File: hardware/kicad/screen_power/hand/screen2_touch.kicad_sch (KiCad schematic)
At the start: 7 parts, among them J201 PI USB / XH4, J202 TOUCH / XH4, K201 IM02TS, Q201 2N7000

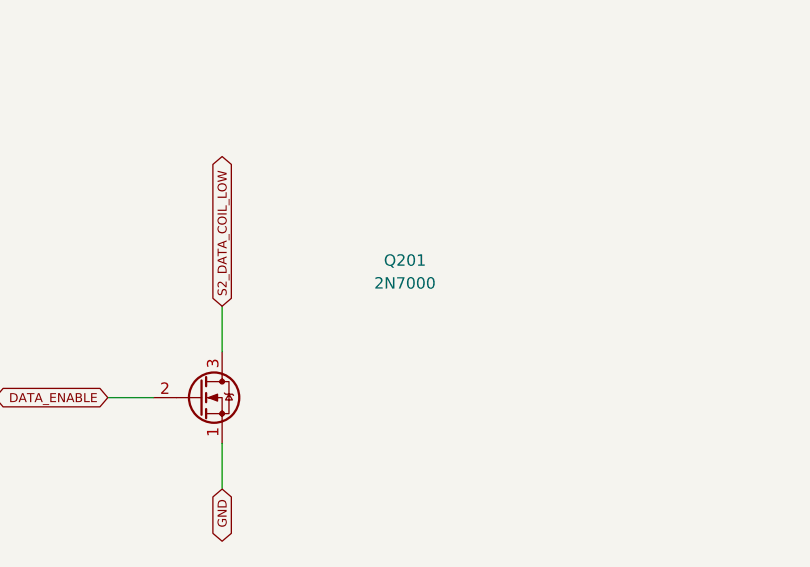
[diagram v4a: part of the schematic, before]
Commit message: fix(hardware): strengthen screen gate drive and finish PCB copper
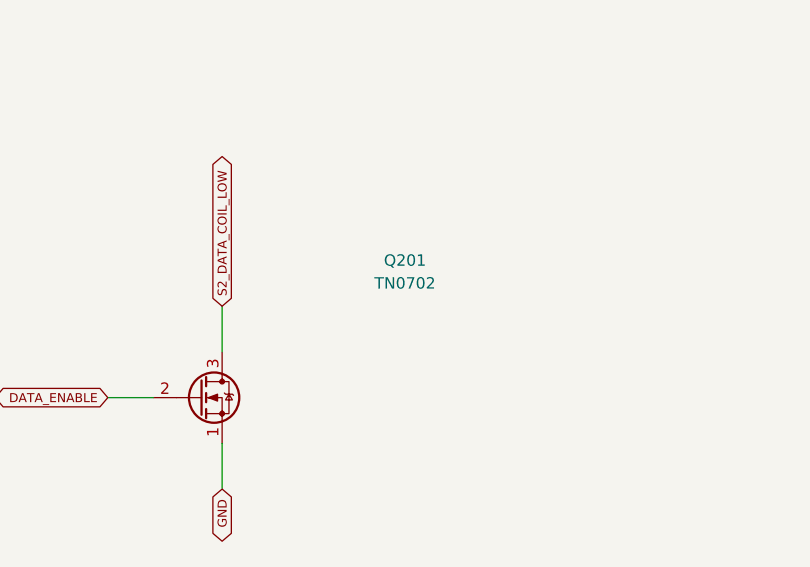
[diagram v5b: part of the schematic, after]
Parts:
- Q201: value 2N7000 -> TN0702; MPN 2N7000 -> TN0702N3-G
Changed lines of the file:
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@@
   (title_block
     (title "Segno screen power / hand / screen2 touch")
-    (rev "K prototype")
+    (rev "L prototype")
     (comment 1 "Discrete 5V switch. Host VBUS powers only its own signal relay coil.")
     (comment 2 "Physical verification required before release."))
@@
         (font
           (size 1.27 1.27))))
-    (property "Value" "2N7000"
+    (property "Value" "TN0702"
       (at 276.86 101.60000000000001 0)
       (effects
@@
           (size 1.27 1.27))
         (hide yes)))
-    (property "MPN" "2N7000"
+    (property "MPN" "TN0702N3-G"
       (at 276.86 114.3 0)
       (effects

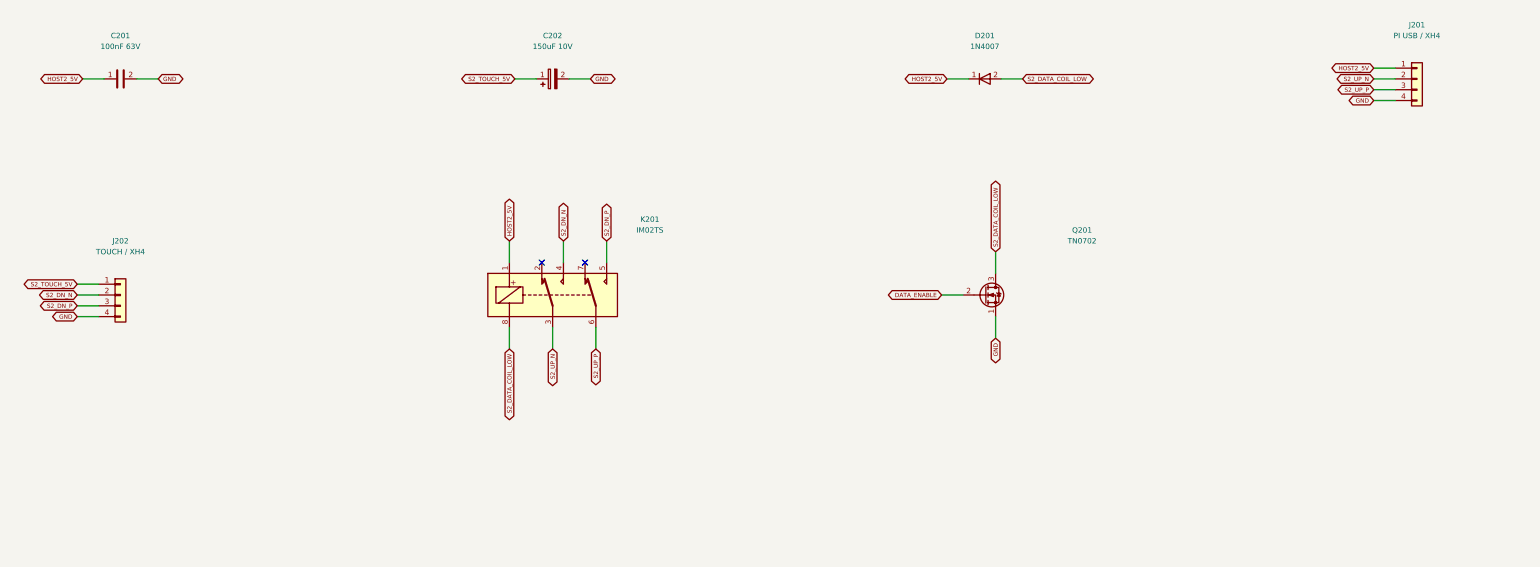
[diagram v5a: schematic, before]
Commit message: fix(hardware): correct USB relay power source and assess revised routing
Prepare Revision M schematic, low-current host sensing and shield drain pads. Keep screen manufacturing on hold pending the revised native layout and complete release validation.
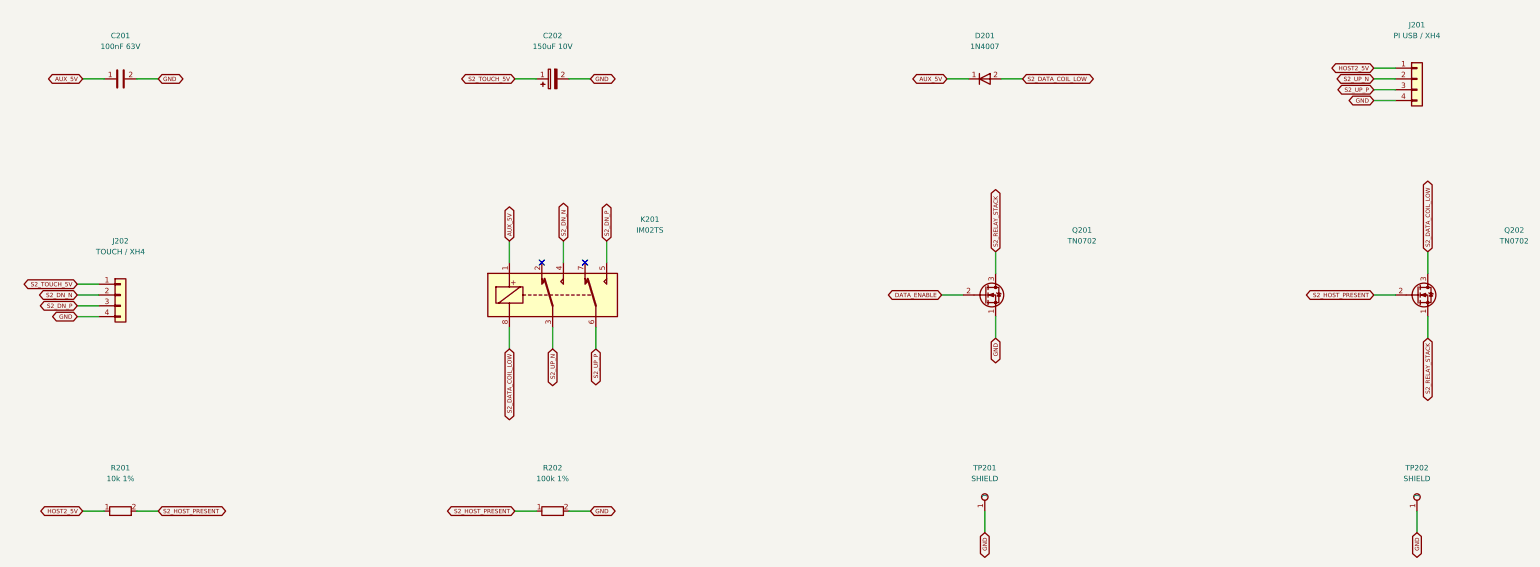
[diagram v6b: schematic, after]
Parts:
- added Q202: TN0702, Package_TO_SOT_THT:TO-92_Inline_Wide, symbol screen_symbols:Transistor_FET_2N7000
- added R201: 10k 1%, Resistor_THT:R_Axial_DIN0207_L6.3mm_D2.5mm_P10.16mm_Horizontal, symbol screen_symbols:Device_R
- added R202: 100k 1%, Resistor_THT:R_Axial_DIN0207_L6.3mm_D2.5mm_P10.16mm_Horizontal, symbol screen_symbols:Device_R
- added TP201, TP202: SHIELD, TestPoint:TestPoint_THTPad_D2.0mm_Drill1.0mm, symbol screen_symbols:Connector_TestPoint
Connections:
- net GND: now also R202.2, TP201.1, TP202.1
- net HOST2_5V: now also R201.1; no longer C201.1, D201.1 (K), K201.1
- net S2_DATA_COIL_LOW: now also Q202.3 (D); no longer Q201.3 (D)
- new net AUX_5V: C201.1, D201.1 (K), K201.1
- new net S2_HOST_PRESENT: Q202.2 (G), R201.2, R202.1
- new net S2_RELAY_STACK: Q201.3 (D), Q202.1 (S)

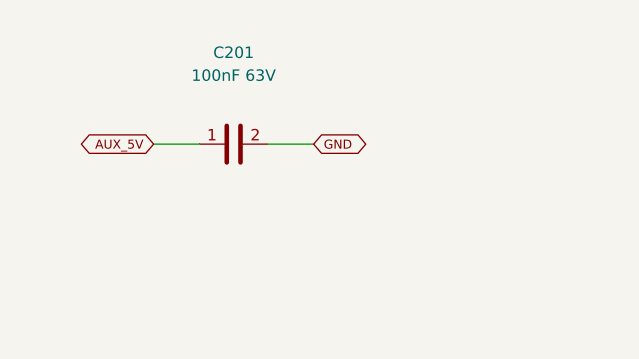
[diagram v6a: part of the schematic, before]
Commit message: feat(hardware): lower screen power cost and finish copper contours
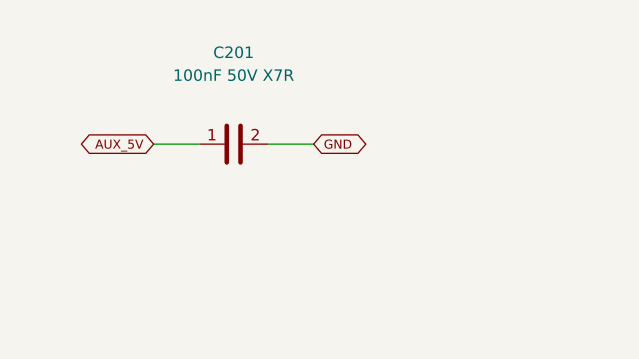
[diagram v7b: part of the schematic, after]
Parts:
- C201: value 100nF 63V -> 100nF 50V X7R; footprint Capacitor_THT:C_Rect_L7.2mm_W2.5mm_P5.00mm -> Capacitor_THT:C_Disc_D7.5mm_W4.4mm_P5.00mm; MPN MKS2C031001A00KSSD -> K104K10X7RF53H5
- D201: MPN 1N4007-E3/54 -> 1N4007G
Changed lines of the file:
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@@
   (title_block
     (title "Segno screen power / hand / screen2 touch")
-    (rev "M prototype")
-    (comment 1 "AUX-powered relays; each host VBUS supplies only its presence detector.")
-    (comment 2 "Physical verification required before release."))
+    (rev "N prototype")
+    (comment 1 "One normally open contact switches AUX; every board load sits behind F1.")
+    (comment 2 "AUX-powered relays; each host VBUS supplies only its presence detector.")
+    (comment 3 "Physical verification required before release."))
   (wire
     (pts
@@
         (font
           (size 1.27 1.27))))
-    (property "Value" "100nF 63V"
+    (property "Value" "100nF 50V X7R"
       (at 50.8 55.88 90)
       (effects
         (font
           (size 1.27 1.27))))
-    (property "Footprint" "Capacitor_THT:C_Rect_L7.2mm_W2.5mm_P5.00mm"
+    (property "Footprint" "Capacitor_THT:C_Disc_D7.5mm_W4.4mm_P5.00mm"
       (at 50.8 63.5 90)
       (effects
@@
           (size 1.27 1.27))
         (hide yes)))
-    (property "MPN" "MKS2C031001A00KSSD"
+    (property "MPN" "K104K10X7RF53H5"
       (at 50.8 63.5 90)
       (effects
@@
           (size 1.27 1.27))
         (hide yes)))
-    (property "MPN" "1N4007-E3/54"
+    (property "MPN" "1N4007G"
       (at 254.0 63.5 0)
       (effects

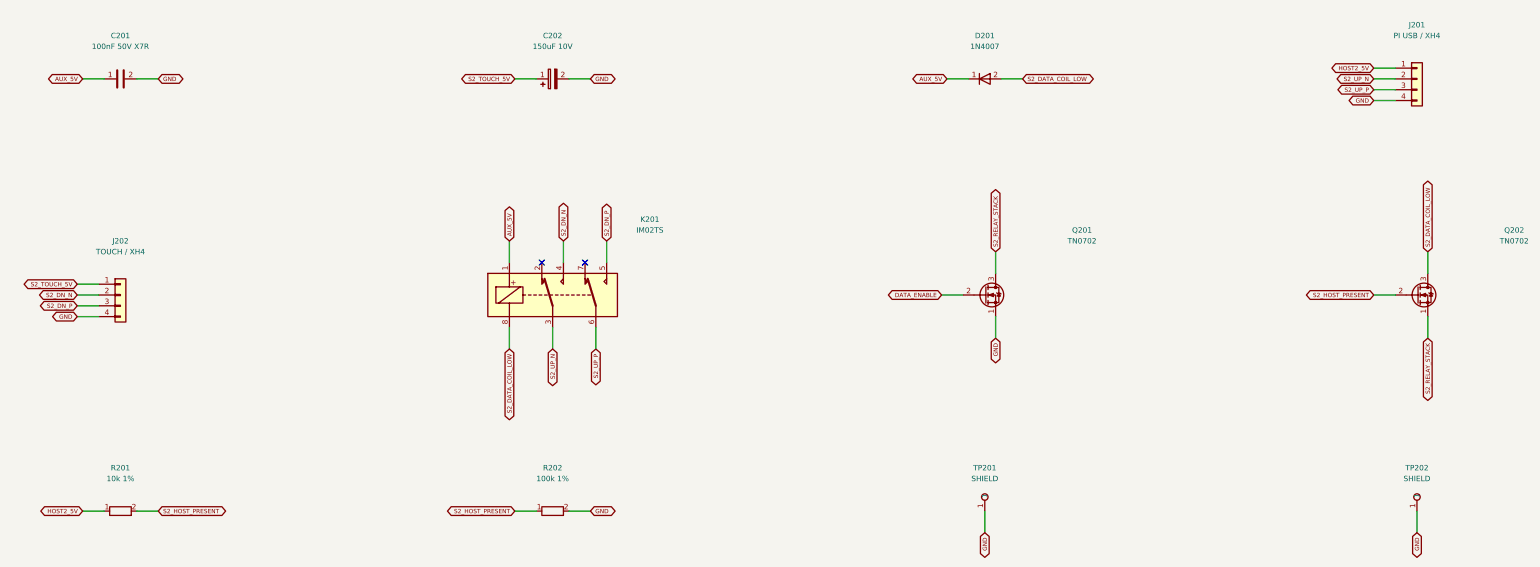
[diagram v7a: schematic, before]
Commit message: feat(hardware): carry USB shields through removable XH5 plugs
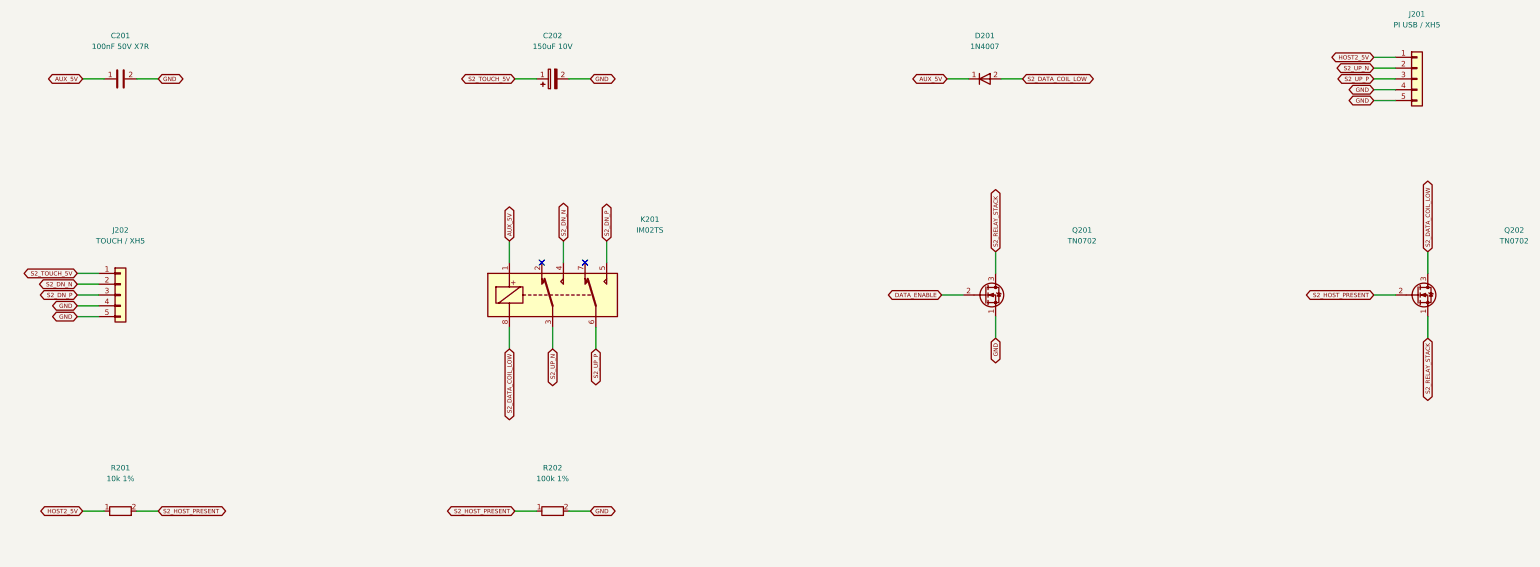
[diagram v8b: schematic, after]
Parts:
- removed TP201, TP202: SHIELD, TestPoint:TestPoint_THTPad_D2.0mm_Drill1.0mm, symbol screen_symbols:Connector_TestPoint
- J201: value PI USB / XH4 -> PI USB / XH5; footprint Connector_JST:JST_XH_B4B-XH-A_1x04_P2.50mm_Vertical -> Connector_JST:JST_XH_B5B-XH-A_1x05_P2.50mm_Vertical; symbol screen_symbols:Connector_Generic_Conn_01x04 -> screen_symbols:Connector_Generic_Conn_01x05; MPN B4B-XH-A(LF)(SN) -> B5B-XH-A(LF)(SN)
- J202: value TOUCH / XH4 -> TOUCH / XH5; footprint Connector_JST:JST_XH_B4B-XH-A_1x04_P2.50mm_Vertical -> Connector_JST:JST_XH_B5B-XH-A_1x05_P2.50mm_Vertical; symbol screen_symbols:Connector_Generic_Conn_01x04 -> screen_symbols:Connector_Generic_Conn_01x05; MPN B4B-XH-A(LF)(SN) -> B5B-XH-A(LF)(SN)
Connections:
- net GND: now also J201.5 (Pin_5), J202.5 (Pin_5)
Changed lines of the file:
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@@
   (title_block
     (title "Segno screen power / hand / screen2 touch")
-    (rev "N prototype")
+    (rev "O prototype")
     (comment 1 "One normally open contact switches AUX; every board load sits behind F1.")
     (comment 2 "AUX-powered relays; each host VBUS supplies only its presence detector.")
@@
   (wire
     (pts
+      (xy 350.52 58.42)
+      (xy 345.44 58.42))
+    (stroke
+      (width 0)
+      (type default))
+)
+  (global_label "HOST2_5V"
+    (shape bidirectional)
+    (at 345.44 58.42 180)
+    (effects
+      (font
+        (size 1.0 1.0))
+      (justify right))
+)
+  (wire
+    (pts
       (xy 350.52 60.96)
       (xy 345.44 60.96))
@@
       (type default))
 )
-  (global_label "HOST2_5V"
+  (global_label "S2_UP_N"
     (shape bidirectional)
     (at 345.44 60.96 180)
@@
       (type default))
 )
-  (global_label "S2_UP_N"
+  (global_label "S2_UP_P"
     (shape bidirectional)
     (at 345.44 63.5 180)
@@
       (type default))
 )
-  (global_label "S2_UP_P"
+  (global_label "GND"
     (shape bidirectional)
     (at 345.44 66.04 180)
@@
 )
   (symbol
-    (lib_id "screen_symbols:Connector_Generic_Conn_01x04")
+    (lib_id "screen_symbols:Connector_Generic_Conn_01x05")
     (at 355.59999999999997 63.5 0)
     (unit 1)
@@
     (dnp no)
     (property "Reference" "J201"
-      (at 355.59999999999997 50.8 0)
-      (effects
-        (font
-          (size 1.27 1.27))))
-    (property "Value" "PI USB / XH4"
-      (at 355.59999999999997 53.339999999999996 0)
-      (effects
-        (font
-          (size 1.27 1.27))))
-    (property "Footprint" "Connector_JST:JST_XH_B4B-XH-A_1x04_P2.50mm_Vertical"
+      (at 355.59999999999997 48.260000000000005 0)
+      (effects
+        (font
+          (size 1.27 1.27))))
+    (property "Value" "PI USB / XH5"
+      (at 355.59999999999997 50.800000000000004 0)
+      (effects
+        (font
+          (size 1.27 1.27))))
+    (property "Footprint" "Connector_JST:JST_XH_B5B-XH-A_1x05_P2.50mm_Vertical"
       (at 355.59999999999997 63.5 0)
       (effects
@@
           (size 1.27 1.27))
         (hide yes)))
-    (property "MPN" "B4B-XH-A(LF)(SN)"
+    (property "MPN" "B5B-XH-A(LF)(SN)"
       (at 355.59999999999997 63.5 0)
       (effects
@@
 )
     (pin "4"
+)
+    (pin "5"
 )
     (instances
@@
   (wire
     (pts
+      (xy 45.72 109.22)
+      (xy 40.64 109.22))
+    (stroke
+      (width 0)
+      (type default))
+)
+  (global_label "S2_TOUCH_5V"
+    (shape bidirectional)
+    (at 40.64 109.22 180)
+    (effects
+      (font
+        (size 1.0 1.0))
+      (justify right))
+)
+  (wire
+    (pts
       (xy 45.72 111.76)
       (xy 40.64 111.76))
@@
       (type default))
 )
-  (global_label "S2_TOUCH_5V"
+  (global_label "S2_DN_N"
     (shape bidirectional)
     (at 40.64 111.76 180)
@@
       (type default))
 )
-  (global_label "S2_DN_N"
+  (global_label "S2_DN_P"
     (shape bidirectional)
     (at 40.64 114.3 180)
@@
       (type default))
 )
-  (global_label "S2_DN_P"
+  (global_label "GND"
     (shape bidirectional)
     (at 40.64 116.84 180)
@@
 )
   (symbol
-    (lib_id "screen_symbols:Connector_Generic_Conn_01x04")
+    (lib_id "screen_symbols:Connector_Generic_Conn_01x05")
     (at 50.8 114.3 0)
     (unit 1)
@@
     (dnp no)
     (property "Reference" "J202"
-      (at 50.8 101.6 0)
-      (effects
-        (font
-          (size 1.27 1.27))))
-    (property "Value" "TOUCH / XH4"
-      (at 50.8 104.14 0)
-      (effects
-        (font
-          (size 1.27 1.27))))
-    (property "Footprint" "Connector_JST:JST_XH_B4B-XH-A_1x04_P2.50mm_Vertical"
+      (at 50.8 99.06 0)
+      (effects
+        (font
+          (size 1.27 1.27))))
+    (property "Value" "TOUCH / XH5"
+      (at 50.8 101.60000000000001 0)
+      (effects
+        (font
+          (size 1.27 1.27))))
+    (property "Footprint" "Connector_JST:JST_XH_B5B-XH-A_1x05_P2.50mm_Vertical"
       (at 50.8 114.3 0)
       (effects
@@
           (size 1.27 1.27))
         (hide yes)))
-    (property "MPN" "B4B-XH-A(LF)(SN)"
+    (property "MPN" "B5B-XH-A(LF)(SN)"
       (at 50.8 114.3 0)
       (effects
@@
 )
     (pin "4"
+)
+    (pin "5"
 )
     (instances
@@
           (reference "R202")
           (unit 1)))))
-  (wire
-    (pts
-      (xy 254.0 165.1)
-      (xy 254.0 170.18))
-    (stroke
-      (width 0)
-      (type default))
-)
-  (global_label "GND"
-    (shape bidirectional)
-    (at 254.0 170.18 270)
-    (effects
-      (font
-        (size 1.0 1.0))
-      (justify right))
-)
-  (symbol
-    (lib_id "screen_symbols:Connector_TestPoint")
-    (at 254.0 165.1 0)
-    (unit 1)
-    (in_bom no)
-    (on_board yes)
-    (dnp no)
-    (property "Reference" "TP201"
-      (at 254.0 154.94 0)
-      (effects
-        (font
-          (size 1.27 1.27))))
-    (property "Value" "SHIELD"
-      (at 254.0 157.48 0)
-      (effects
-        (font
-          (size 1.27 1.27))))
-    (property "Footprint" "TestPoint:TestPoint_THTPad_D2.0mm_Drill1.0mm"
-      (at 254.0 165.1 0)
-      (effects
-        (font
-          (size 1.27 1.27))
-        (hide yes)))
-    (property "MPN" "PCB pad"
-      (at 254.0 165.1 0)
-      (effects
-        (font
-          (size 1.27 1.27))
-        (hide yes)))
-    (pin "1"
-)
-    (instances
-      (project "screen_power_hand"
-        (path "/63a63dd8-c505-5bb8-8418-5eb0e558e546/54c97e4c-a9b4-50bc-a883-235682587f3a"
-          (reference "TP201")
-          (unit 1)))))
-  (wire
-    (pts
-      (xy 355.6 165.1)
-      (xy 355.6 170.18))
-    (stroke
-      (width 0)
-      (type default))
-)
-  (global_label "GND"
-    (shape bidirectional)
-    (at 355.6 170.18 270)
-    (effects
-      (font
-        (size 1.0 1.0))
-      (justify right))
-)
-  (symbol
-    (lib_id "screen_symbols:Connector_TestPoint")
-    (at 355.59999999999997 165.1 0)
-    (unit 1)
-    (in_bom no)
-    (on_board yes)
-    (dnp no)
-    (property "Reference" "TP202"
-      (at 355.59999999999997 154.94 0)
-      (effects
-        (font
-          (size 1.27 1.27))))
-    (property "Value" "SHIELD"
-      (at 355.59999999999997 157.48 0)
-      (effects
-        (font
-          (size 1.27 1.27))))
-    (property "Footprint" "TestPoint:TestPoint_THTPad_D2.0mm_Drill1.0mm"
-      (at 355.59999999999997 165.1 0)
-      (effects
-        (font
-          (size 1.27 1.27))
-        (hide yes)))
-    (property "MPN" "PCB pad"
-      (at 355.59999999999997 165.1 0)
-      (effects
-        (font
-          (size 1.27 1.27))
-        (hide yes)))
-    (pin "1"
-)
-    (instances
-      (project "screen_power_hand"
-        (path "/63a63dd8-c505-5bb8-8418-5eb0e558e546/54c97e4c-a9b4-50bc-a883-235682587f3a"
-          (reference "TP202")
-          (unit 1)))))
   (embedded_fonts no))
